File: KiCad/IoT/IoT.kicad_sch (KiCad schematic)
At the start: 25 parts, among them J1 Program header, J2 Micro_SD_Card_Det2, J3 USB_C_Receptacle_USB2.0_16P, J4 Conn_01x08_Pin, J5 Conn_01x08_Pin, SW1 SW_Push, SW2 SW_Push, U1 STM32F401RETx

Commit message: updated power schematic
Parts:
- added C28: 4.7u, RF_Converter:Balun_Johanson_1.6x0.8mm, symbol Device:C_Polarized
- added R16: 10k, symbol Device:R
- added TP10, TP11, TP12, TP13, TP14, TP8, TP9: TestPoint_Flag, TestPoint:TestPoint_Pad_2.0x2.0mm, symbol Connector:TestPoint_Flag
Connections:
- net +3V3: now also R16.1, TP14.1
- net GND: now also C28.2
- net SPI1_CS: now also R16.2, TP10.1
- net SPI1_MISO: now also TP12.1
- net SPI1_MOSI: now also TP13.1
- net SPI1_SCK: now also TP11.1
- net UART6_RX: now also TP9.1
- net UART6_TX: now also TP8.1
- net at U1.30 (VCAP1): now also C28.1
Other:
- moved on the sheet: J4, J5

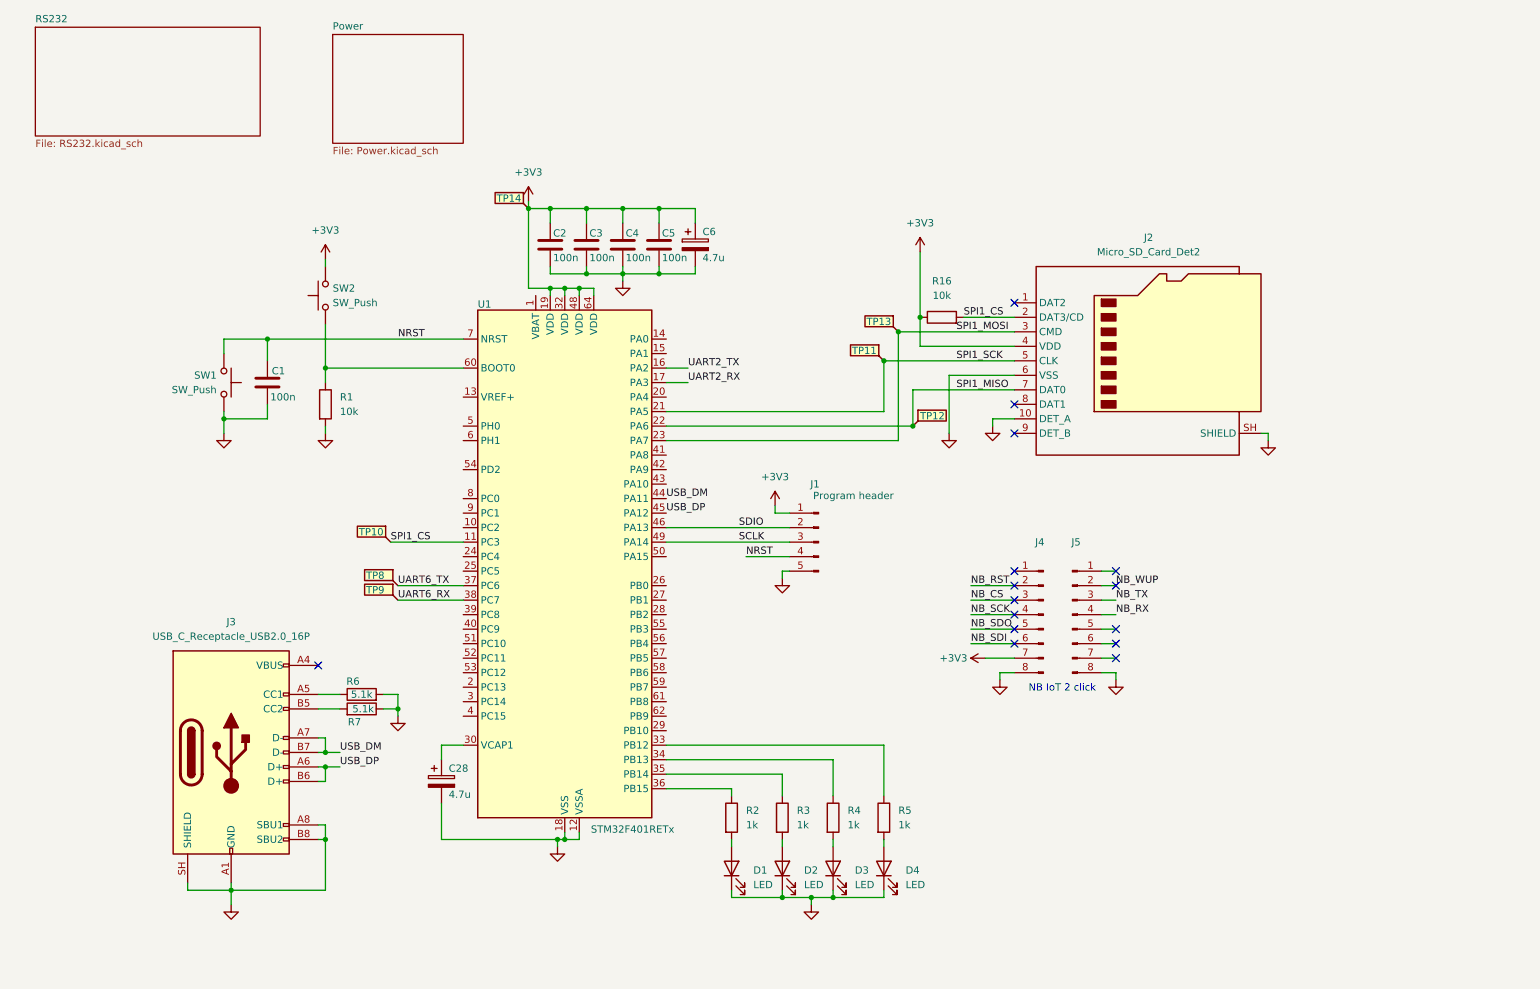
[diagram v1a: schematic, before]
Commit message: added buttons, connected leds, changed uart ic and added crystals
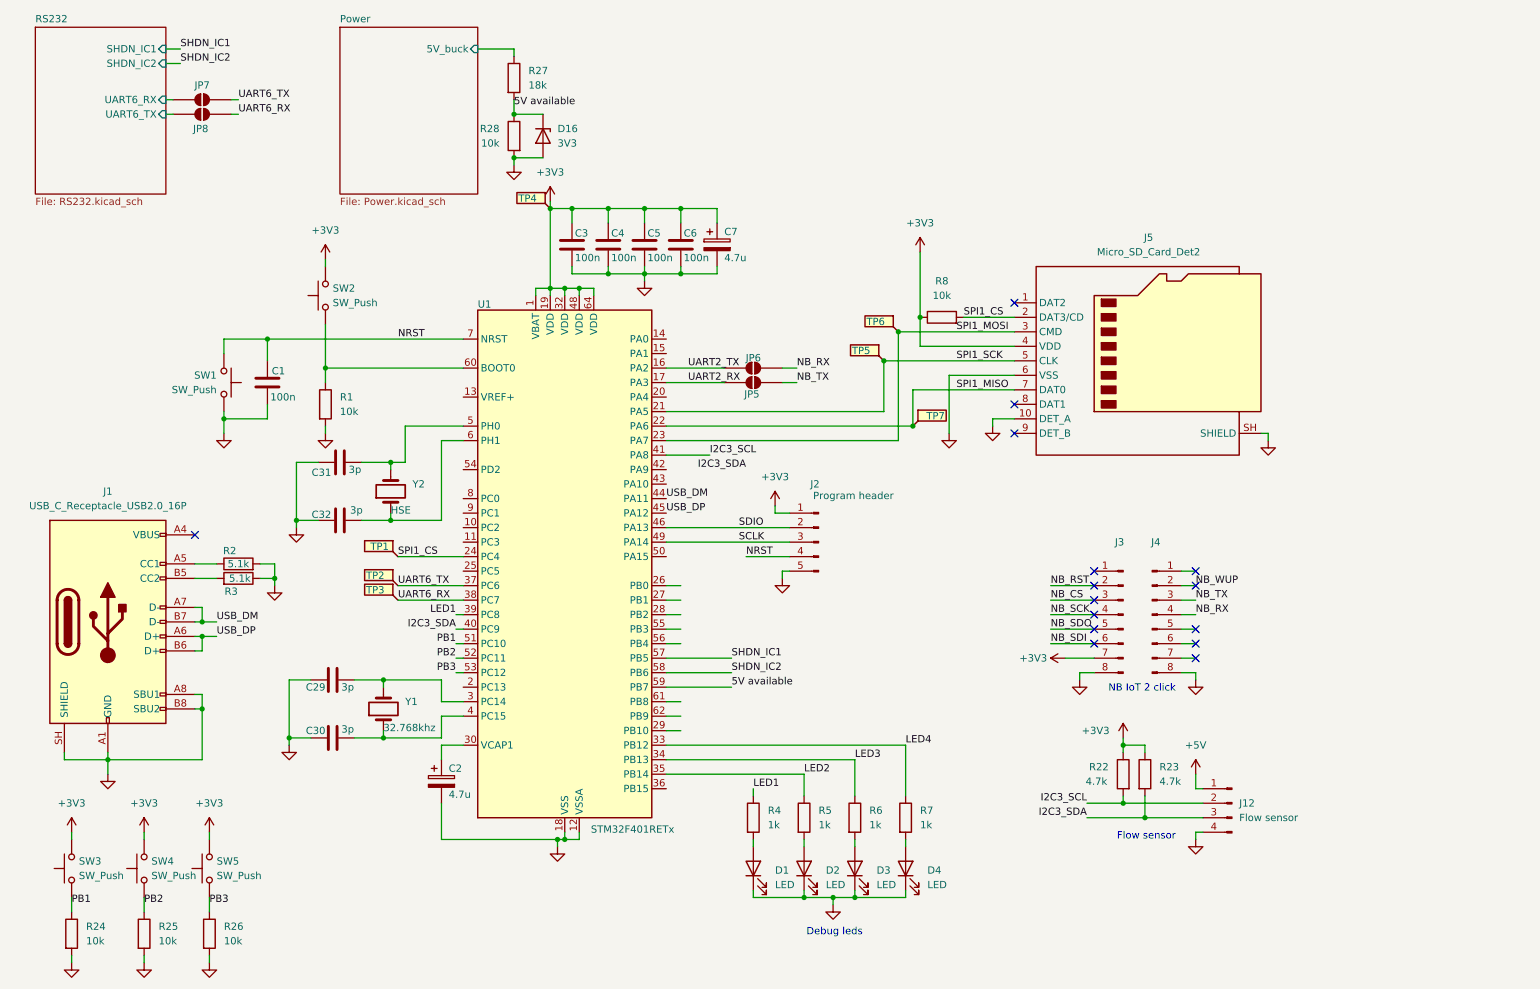
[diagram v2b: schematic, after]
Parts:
- added C29, C30, C31, C32: 3p, Capacitor_SMD:C_0603_1608Metric, symbol Device:C
- added D16: 3V3, symbol Device:D_Zener
- added J12: Flow sensor, Package_SO:TSSOP-8_3x3mm_P0.65mm, symbol Connector:Conn_01x04_Pin
- added JP5, JP6, JP7, JP8: SolderJumper_2_Open, symbol Jumper:SolderJumper_2_Open
- added R22, R23: 4.7k, symbol Device:R
- added R24, R25, R26, R28: 10k, symbol Device:R
- added R27: 18k, symbol Device:R
- added SW3, SW4, SW5: SW_Push, Package_SO:TSSOP-20_4.4x6.5mm_P0.65mm, symbol Switch:SW_Push
- added Y1: 32.768khz, symbol Device:Crystal
- added Y2: HSE, symbol Device:Crystal
- C1: footprint (none) -> Capacitor_SMD:C_0201_0603Metric_Pad0.64x0.40mm_HandSolder
- C2: renamed from C28; footprint RF_Converter:Balun_Johanson_1.6x0.8mm -> (none)
- C3: renamed from C2; footprint (none) -> Capacitor_SMD:C_0603_1608Metric_Pad1.08x0.95mm_HandSolder
- C4: renamed from C3; footprint (none) -> Capacitor_SMD:C_0603_1608Metric_Pad1.08x0.95mm_HandSolder
- C5: renamed from C4; footprint (none) -> Capacitor_SMD:C_0603_1608Metric_Pad1.08x0.95mm_HandSolder
- C6: renamed from C5; footprint (none) -> Capacitor_SMD:C_0603_1608Metric_Pad1.08x0.95mm_HandSolder
- C7: renamed from C6; footprint RF_Converter:Balun_Johanson_1.6x0.8mm -> (none)
- D1, D2, D3, D4: footprint LED_SMD:LED_Cree-XHP50_3V_HighDensity -> (none)
- renumbered J3 to J1, J1 to J2, J4 to J3, J5 to J4, J2 to J5, R6 to R2, R7 to R3, R2 to R4, R3 to R5, R4 to R6, R5 to R7, R16 to R8, TP10 to TP1, TP8 to TP2, TP9 to TP3, TP14 to TP4, TP11 to TP5, TP13 to TP6, TP12 to TP7
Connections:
- net +3V3: now also U1.1 (VBAT), R22.1, R23.1, SW3.2, SW4.2, SW5.2
- net GND: now also C29.1, C30.1, C31.1, C32.1, D16.2 (A), J12.4 (Pin_4), R24.2, R25.2, R26.2, R28.2
- net NB_RX: now also JP6.2 (B)
- net NB_TX: now also JP5.2 (B)
- net SPI1_CS: now also U1.24 (PC4); no longer U1.11 (PC3)
- net UART2_RX: now also JP5.1 (A)
- net UART2_TX: now also JP6.1 (A)
- net UART6_RX: now also JP8.2 (B)
- net UART6_TX: now also JP7.2 (B)
- net LED4: now reaches R7.1, U1.33 (PB12)
- net at U1.3 (PC14): now also C29.2, Y1.2
- net LED3: now reaches R6.1, U1.34 (PB13)
- net LED2: now reaches R5.1, U1.35 (PB14)
- net at U1.36 (PB15): no longer R4.1
- net LED1: now reaches U1.39 (PC8)
- net LED1: now also R4.1
- net at U1.4 (PC15): now also C30.2, Y1.1
- net I2C3_SDA: now reaches U1.40 (PC9)
- net I2C3_SDA: now also J12.3 (Pin_3), R23.2
- net I2C3_SCL: now reaches U1.41 (PA8)
- net I2C3_SCL: now also J12.2 (Pin_2), R22.2
- net at U1.5 (PH0): now also C31.2, Y2.2
- net PB1: now reaches U1.51 (PC10)
- net PB1: now also R24.1, SW3.1
- net PB2: now reaches U1.52 (PC11)
- net PB2: now also R25.1, SW4.1
- net PB3: now reaches U1.53 (PC12)
- net PB3: now also R26.1, SW5.1
- net SHDN_IC1: now reaches U1.57 (PB5)
- net SHDN_IC2: now reaches U1.58 (PB6)
- net 5V available: now reaches U1.59 (PB7)
- net 5V available: now also D16.1 (K), R27.2, R28.1
- net at U1.6 (PH1): now also C32.2, Y2.1
- new net +5V: J12.1 (Pin_1)
- new net Power/5V_buck: R27.1
- new net RS232/UART6_RX: JP7.1 (A)
- new net RS232/UART6_TX: JP8.1 (A)
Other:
- sheet Power ports: added 5V_buck; removed none
- sheet RS232 ports: added SHDN_IC1, SHDN_IC2, UART6_RX, UART6_TX; removed none
- note added: "Debug leds"
- note added: "Flow sensor"
- moved on the sheet: C3, C4, C5, C6, C7, D1, D2, D3, D4, J1, J3, J4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

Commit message: minor fixes and cleanup
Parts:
- added C11: 100n, Capacitor_SMD:C_0603_1608Metric_Pad1.08x0.95mm_HandSolder, symbol Device:C
- renumbered C6 to C10, C7 to C12, C29 to C2, C30 to C3, C31 to C4, C32 to C5, C2 to C6, C3 to C7, C4 to C8, C5 to C9, D16 to D1, D1 to D2, D2 to D3, D3 to D4, D4 to D5, J5 to J4, J4 to J5, J12 to J6, JP7 to JP1, JP8 to JP2, JP6 to JP3, JP5 to JP4, R24 to R1, R5 to R10, R6 to R11, R7 to R12, R8 to R13, R22 to R14, R23 to R15, R25 to R2, R26 to R3, R2 to R4, R3 to R5, R1 to R6, R27 to R7, R28 to R8, R4 to R9, SW3 to SW1, SW4 to SW2, SW5 to SW3, SW1 to SW4, SW2 to SW5
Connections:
- net +3V3: now also C11.1
- net GND: now also C11.2
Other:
- moved on the sheet: C12
